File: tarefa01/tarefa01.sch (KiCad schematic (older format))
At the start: 18 parts, among them U1 nrf52832, X1 32MHz, X2 32.768kHz

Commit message: add footprint
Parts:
- C1, C10, C11, C12, C2, C3, C5, C7, C8, C9: footprint (none) -> Capacitor_SMD:C_0201_0603Metric
- C4: footprint (none) -> Capacitor_SMD:C_0603_1608Metric_Pad1.05x0.95mm_HandSolder
- C6: footprint (none) -> Capacitor_SMD:C_0402_1005Metric
- L1: footprint (none) -> Inductor_SMD:L_0402_1005Metric
- L2: footprint (none) -> Inductor_SMD:L_0603_1608Metric_Pad1.05x0.95mm_HandSolder
- L3: footprint (none) -> Inductor_SMD:L_0201_0603Metric
- U1: footprint (none) -> tarefa01:QFN-48_EP_6x6_Pitch0.4mm; symbol My-Schematic-Library:nrf52832 -> tarefa01-rescue:nrf52832-My-Schematic-Library
- X1: footprint (none) -> Crystal:Crystal_SMD_2016-4Pin_2.0x1.6mm
- X2: footprint (none) -> Crystal:Crystal_SMD_2012-2Pin_2.0x1.2mm_HandSoldering
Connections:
- net Earth: now also U1.49 (DiePad)
- no-connect marks 34 -> 33
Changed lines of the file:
@@
 EESchema Schematic File Version 4
+LIBS:tarefa01-cache
 EELAYER 29 0
 EELAYER END
@@
 $EndDescr
 $Comp
-L My-Schematic-Library:nrf52832 U1
+L tarefa01-rescue:nrf52832-My-Schematic-Library U1
 U 1 1 5CF3EA1E
 P 5300 3750
 F 0 "U1" H 4400 4750 50  0000 L CNN
 F 1 "nrf52832" H 4350 4650 50  0000 L CNN
-F 2 "" H 4900 3450 50  0001 C CNN
+F 2 "tarefa01:QFN-48_EP_6x6_Pitch0.4mm" H 4900 3450 50  0001 C CNN
 F 3 "" H 4900 3450 50  0001 C CNN
 	1    5300 3750
@@
 F 0 "C1" V 2698 2950 50  0000 C CNN
 F 1 "12pF" V 2789 2950 50  0000 C CNN
-F 2 "" H 2988 2800 50  0001 C CNN
+F 2 "Capacitor_SMD:C_0201_0603Metric" H 2988 2800 50  0001 C CNN
 F 3 "~" H 2950 2950 50  0001 C CNN
 	1    2950 2950
@@
 F 0 "C2" V 2698 3450 50  0000 C CNN
 F 1 "12pF" V 2789 3450 50  0000 C CNN
-F 2 "" H 2988 3300 50  0001 C CNN
+F 2 "Capacitor_SMD:C_0201_0603Metric" H 2988 3300 50  0001 C CNN
 F 3 "~" H 2950 3450 50  0001 C CNN
 	1    2950 3450
@@
 F 0 "X2" V 3304 3331 50  0000 L CNN
 F 1 "32.768kHz" V 3395 3331 50  0000 L CNN
-F 2 "" H 3350 3200 50  0001 C CNN
+F 2 "Crystal:Crystal_SMD_2012-2Pin_2.0x1.2mm_HandSoldering" H 3350 3200 50  0001 C CNN
 F 3 "~" H 3350 3200 50  0001 C CNN
 	1    3350 3200
@@
 F 0 "C3" V 4150 2650 50  0000 C CNN
 F 1 "100nF" V 4250 2650 50  0000 C CNN
-F 2 "" H 4038 2500 50  0001 C CNN
+F 2 "Capacitor_SMD:C_0201_0603Metric" H 4038 2500 50  0001 C CNN
 F 3 "~" H 4000 2650 50  0001 C CNN
 	1    4000 2650
@@
 F 0 "C4" V 4750 2350 50  0000 C CNN
 F 1 "4.7uF" V 4850 2350 50  0000 C CNN
-F 2 "" H 4638 2200 50  0001 C CNN
+F 2 "Capacitor_SMD:C_0603_1608Metric_Pad1.05x0.95mm_HandSolder" H 4638 2200 50  0001 C CNN
 F 3 "~" H 4600 2350 50  0001 C CNN
 	1    4600 2350
@@
 $EndComp
 Wire Wire Line
-	4600 2650 4600 2500
+	4600 2650 4600 2600
 Wire Wire Line
 	4850 2850 4850 2100
@@
 F 0 "C6" V 5200 1750 50  0000 C CNN
 F 1 "1.0uF" V 5100 1750 50  0000 C CNN
-F 2 "" H 5388 1600 50  0001 C CNN
+F 2 "Capacitor_SMD:C_0402_1005Metric" H 5388 1600 50  0001 C CNN
 F 3 "~" H 5350 1750 50  0001 C CNN
 	1    5350 1750
@@
 F 0 "L1" V 4904 1578 50  0000 L CNN
 F 1 "15nH" H 5000 1650 50  0000 L CNN
-F 2 "" H 4950 1500 50  0001 C CNN
+F 2 "Inductor_SMD:L_0402_1005Metric" H 4950 1500 50  0001 C CNN
 F 3 "~" H 4950 1500 50  0001 C CNN
 	1    4950 1500
@@
 F 0 "L2" V 4904 2228 50  0000 L CNN
 F 1 "10uH" H 5000 2300 50  0000 L CNN
-F 2 "" H 4950 2150 50  0001 C CNN
+F 2 "Inductor_SMD:L_0603_1608Metric_Pad1.05x0.95mm_HandSolder" H 4950 2150 50  0001 C CNN
 F 3 "~" H 4950 2150 50  0001 C CNN
 	1    4950 2150
@@
 F 0 "C5" V 4850 5250 50  0000 C CNN
 F 1 "100nF" V 4950 5250 50  0000 C CNN
-F 2 "" H 4738 5100 50  0001 C CNN
+F 2 "Capacitor_SMD:C_0201_0603Metric" H 4738 5100 50  0001 C CNN
 F 3 "~" H 4700 5250 50  0001 C CNN
 	1    4700 5250
@@
 F 0 "C8" V 7050 4000 50  0000 C CNN
 F 1 "0.8pF" V 7150 4000 50  0000 C CNN
-F 2 "" H 6938 3850 50  0001 C CNN
+F 2 "Capacitor_SMD:C_0201_0603Metric" H 6938 3850 50  0001 C CNN
 F 3 "~" H 6900 4000 50  0001 C CNN
 	1    6900 4000
@@
 F 0 "L3" V 7304 3928 50  0000 L CNN
 F 1 "3.9nH" H 7200 3750 50  0000 L CNN
-F 2 "" H 7350 3850 50  0001 C CNN
+F 2 "Inductor_SMD:L_0201_0603Metric" H 7350 3850 50  0001 C CNN
 F 3 "~" H 7350 3850 50  0001 C CNN
 	1    7350 3850
@@
 F 0 "C12" V 7500 3550 50  0000 C CNN
 F 1 "N.C." V 7600 3550 50  0000 C CNN
-F 2 "" H 7388 3400 50  0001 C CNN
+F 2 "Capacitor_SMD:C_0201_0603Metric" H 7388 3400 50  0001 C CNN
 F 3 "~" H 7350 3550 50  0001 C CNN
 	1    7350 3550
@@
 F 0 "C11" V 7500 3200 50  0000 C CNN
 F 1 "100pF" V 7600 3200 50  0000 C CNN
-F 2 "" H 7388 3050 50  0001 C CNN
+F 2 "Capacitor_SMD:C_0201_0603Metric" H 7388 3050 50  0001 C CNN
 F 3 "~" H 7350 3200 50  0001 C CNN
 	1    7350 3200
@@
 F 0 "C10" V 7500 2850 50  0000 C CNN
 F 1 "12pF" V 7600 2850 50  0000 C CNN
-F 2 "" H 7388 2700 50  0001 C CNN
+F 2 "Capacitor_SMD:C_0201_0603Metric" H 7388 2700 50  0001 C CNN
 F 3 "~" H 7350 2850 50  0001 C CNN
 	1    7350 2850
@@
 F 0 "C9" V 7500 2400 50  0000 C CNN
 F 1 "12pF" V 7600 2400 50  0000 C CNN
-F 2 "" H 7388 2250 50  0001 C CNN
+F 2 "Capacitor_SMD:C_0201_0603Metric" H 7388 2250 50  0001 C CNN
 F 3 "~" H 7350 2400 50  0001 C CNN
 	1    7350 2400
@@
 F 0 "C7" V 6650 2300 50  0000 C CNN
 F 1 "100nF" V 6300 2300 50  0000 C CNN
-F 2 "" H 6538 2150 50  0001 C CNN
+F 2 "Capacitor_SMD:C_0201_0603Metric" H 6538 2150 50  0001 C CNN
 F 3 "~" H 6500 2300 50  0001 C CNN
 	1    6500 2300
@@
 F 0 "X1" V 6854 2731 50  0000 L CNN
 F 1 "32MHz" V 6945 2731 50  0000 L CNN
-F 2 "" H 6900 2600 50  0001 C CNN
+F 2 "Crystal:Crystal_SMD_2016-4Pin_2.0x1.6mm" H 6900 2600 50  0001 C CNN
 F 3 "~" H 6900 2600 50  0001 C CNN
 	1    6900 2600
@@
 NoConn ~ 4200 3650
 NoConn ~ 4200 3550
-NoConn ~ 4750 2850
+Wire Wire Line
+	4750 2850 4750 2600
+Wire Wire Line
+	4750 2600 4600 2600
+Connection ~ 4600 2600
+Wire Wire Line
+	4600 2600 4600 2500
 $EndSCHEMATC

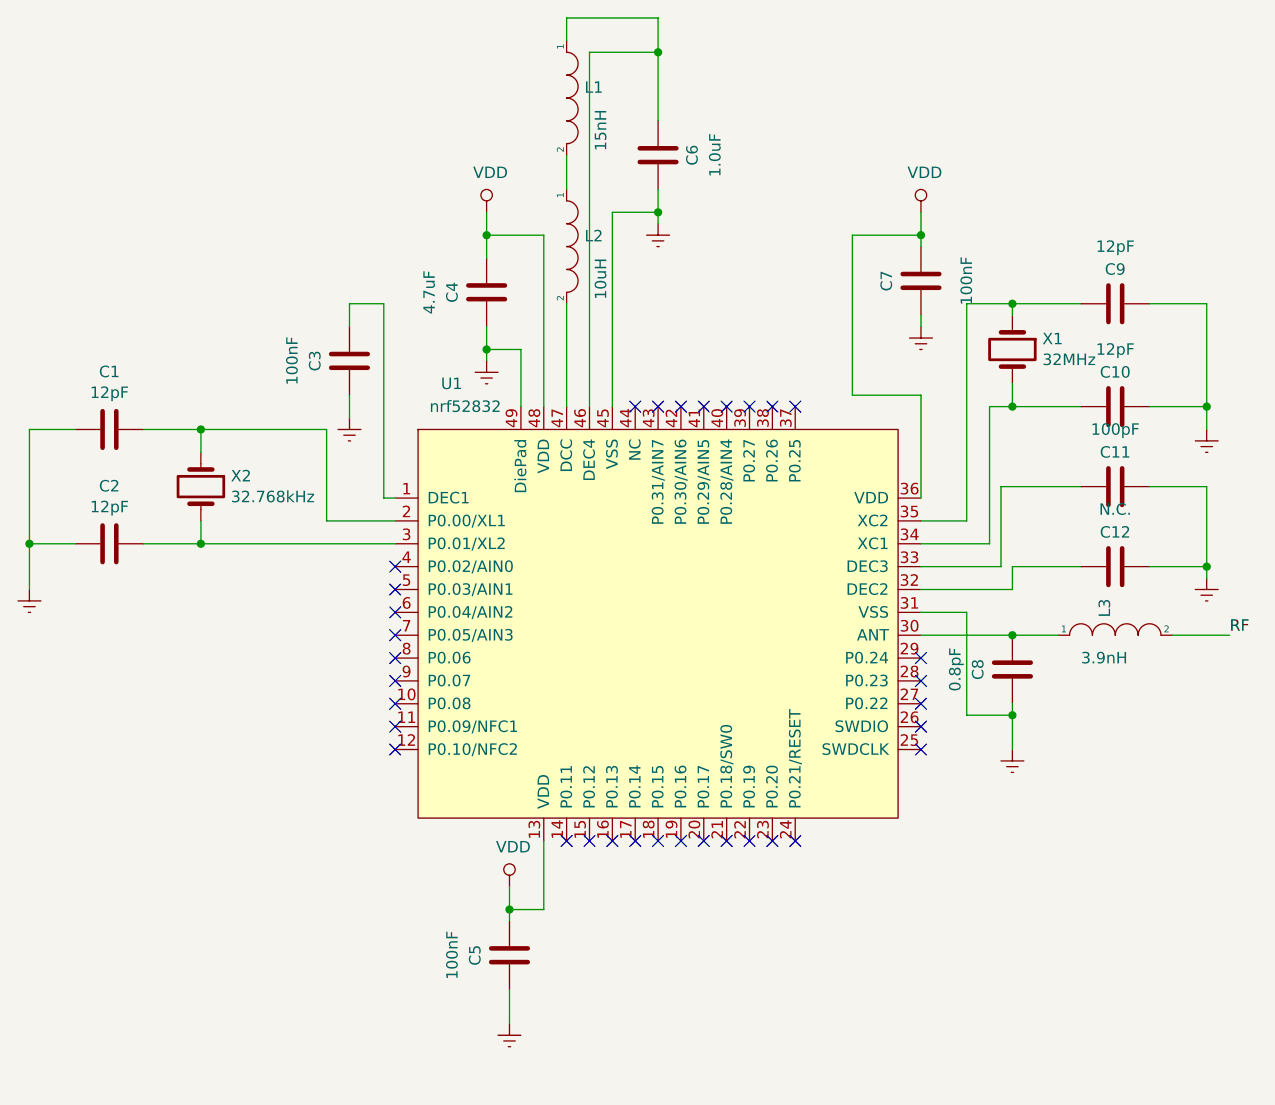
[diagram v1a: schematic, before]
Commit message: Resolvendo erros do esquemático
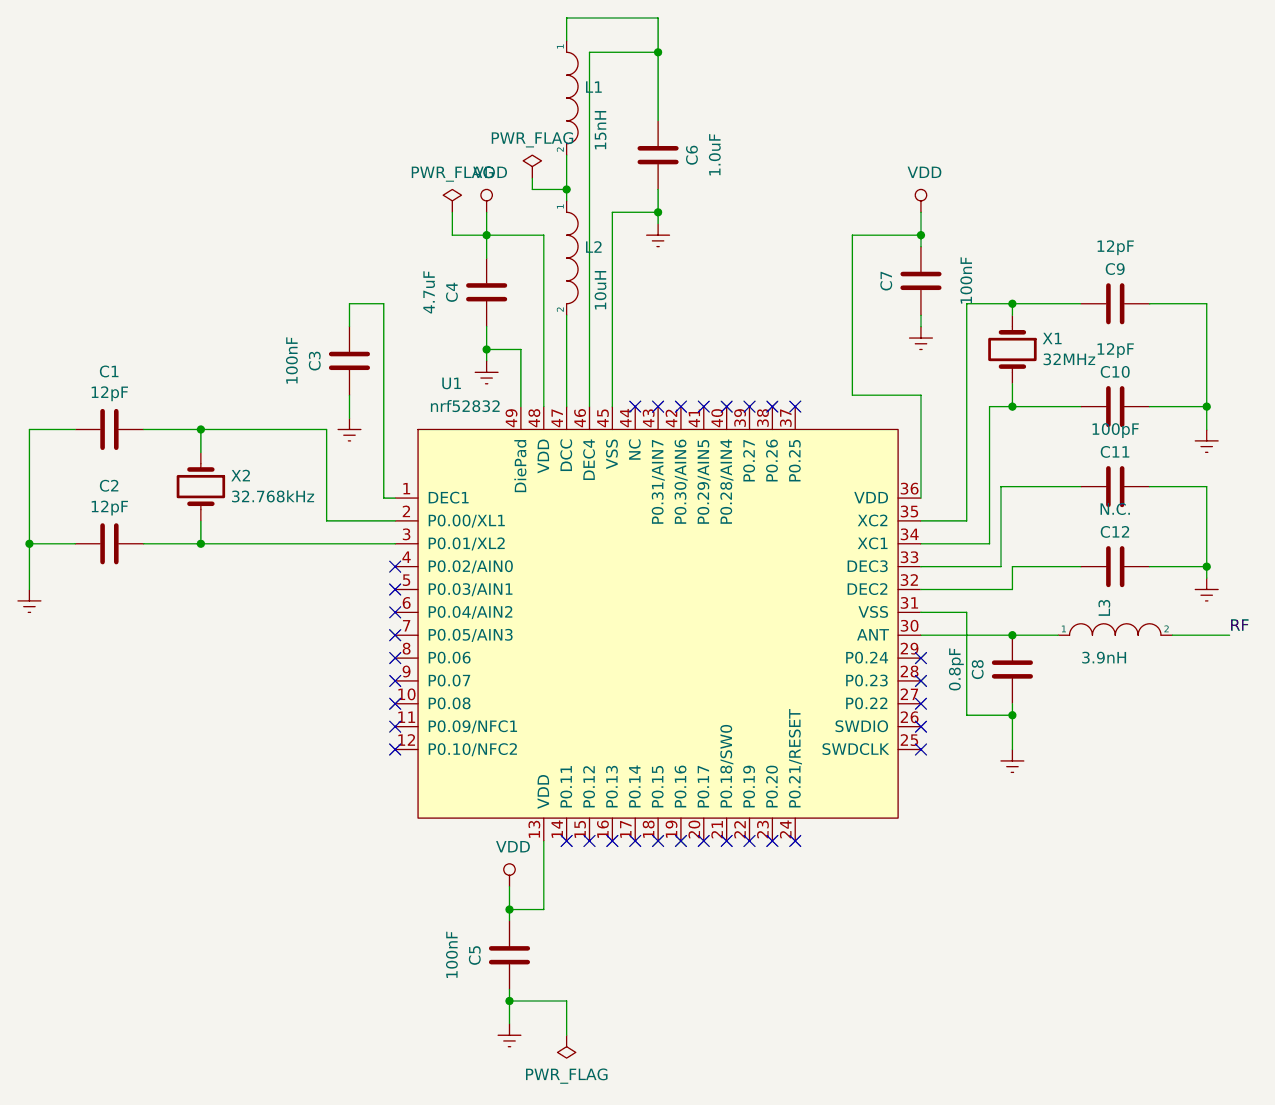
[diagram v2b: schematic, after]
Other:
- moved on the sheet: L2
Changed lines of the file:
@@
 	4850 2850 4850 2100
-Wire Wire Line
-	4850 2100 4600 2100
 Wire Wire Line
 	4600 2100 4600 2200
@@
 L pspice:INDUCTOR L2
 U 1 1 5CF5C67D
-P 4950 2150
-F 0 "L2" V 4904 2228 50  0000 L CNN
-F 1 "10uH" H 5000 2300 50  0000 L CNN
-F 2 "Inductor_SMD:L_0603_1608Metric_Pad1.05x0.95mm_HandSolder" H 4950 2150 50  0001 C CNN
-F 3 "~" H 4950 2150 50  0001 C CNN
-	1    4950 2150
+P 4950 2200
+F 0 "L2" V 4904 2278 50  0000 L CNN
+F 1 "10uH" H 5000 2350 50  0000 L CNN
+F 2 "Inductor_SMD:L_0603_1608Metric_Pad1.05x0.95mm_HandSolder" H 4950 2200 50  0001 C CNN
+F 3 "~" H 4950 2200 50  0001 C CNN
+	1    4950 2200
 	0    1    1    0
 $EndComp
 Wire Wire Line
-	4950 1900 4950 1750
-Wire Wire Line
 	4950 1250 4950 1150
 Wire Wire Line
@@
 	5350 2050 5350 2000
 Wire Wire Line
-	4950 2400 4950 2850
+	4950 2450 4950 2850
 Wire Wire Line
 	5050 2850 5050 1300
@@
 	4700 5050 4700 5100
 Wire Wire Line
-	4700 5400 4700 5550
+	4700 5400 4700 5450
 $Comp
 L Device:C C8
@@
 Wire Wire Line
 	4600 2600 4600 2500
+Wire Wire Line
+	4850 2100 4600 2100
+Wire Wire Line
+	4450 2100 4450 2000
+$Comp
+L power:PWR_FLAG #FLG0101
+U 1 1 5CF99027
+P 4450 2000
+F 0 "#FLG0101" H 4450 2075 50  0001 C CNN
+F 1 "PWR_FLAG" H 4450 2173 50  0000 C CNN
+F 2 "" H 4450 2000 50  0001 C CNN
+F 3 "~" H 4450 2000 50  0001 C CNN
+	1    4450 2000
+	1    0    0    -1
+$EndComp
+Wire Wire Line
+	4450 2100 4600 2100
+$Comp
+L power:PWR_FLAG #FLG0102
+U 1 1 5CFCC117
+P 4950 5600
+F 0 "#FLG0102" H 4950 5675 50  0001 C CNN
+F 1 "PWR_FLAG" H 4950 5773 50  0000 C CNN
+F 2 "" H 4950 5600 50  0001 C CNN
+F 3 "~" H 4950 5600 50  0001 C CNN
+	1    4950 5600
+	-1   0    0    1
+$EndComp
+Wire Wire Line
+	4950 5600 4950 5450
+Wire Wire Line
+	4950 5450 4700 5450
+Connection ~ 4700 5450
+Wire Wire Line
+	4700 5450 4700 5550
+Wire Wire Line
+	4950 1950 4950 1900
+$Comp
+L power:PWR_FLAG #FLG0103
+U 1 1 5CFF271E
+P 4800 1850
+F 0 "#FLG0103" H 4800 1925 50  0001 C CNN
+F 1 "PWR_FLAG" H 4800 2023 50  0000 C CNN
+F 2 "" H 4800 1850 50  0001 C CNN
+F 3 "~" H 4800 1850 50  0001 C CNN
+	1    4800 1850
+	1    0    0    -1
+$EndComp
+Wire Wire Line
+	4950 1900 4800 1900
+Wire Wire Line
+	4800 1900 4800 1850
+Connection ~ 4950 1900
+Wire Wire Line
+	4950 1900 4950 1750
 $EndSCHEMATC
